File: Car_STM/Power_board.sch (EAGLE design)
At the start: 38 parts, among them K1 G2RE, K10 HY1-12V, K11 HY1-12V, K12 G2RE, K13 G2RE, K14 TF2-L2-9V, K2 HY1-12V, K3 TF2-L2-9V, K4 S22, K5 S22, K6 S22, K7 S22, K8 S22, K9 S22, X11 1751248, X13 1751248, X17 1751251, X18 1751251

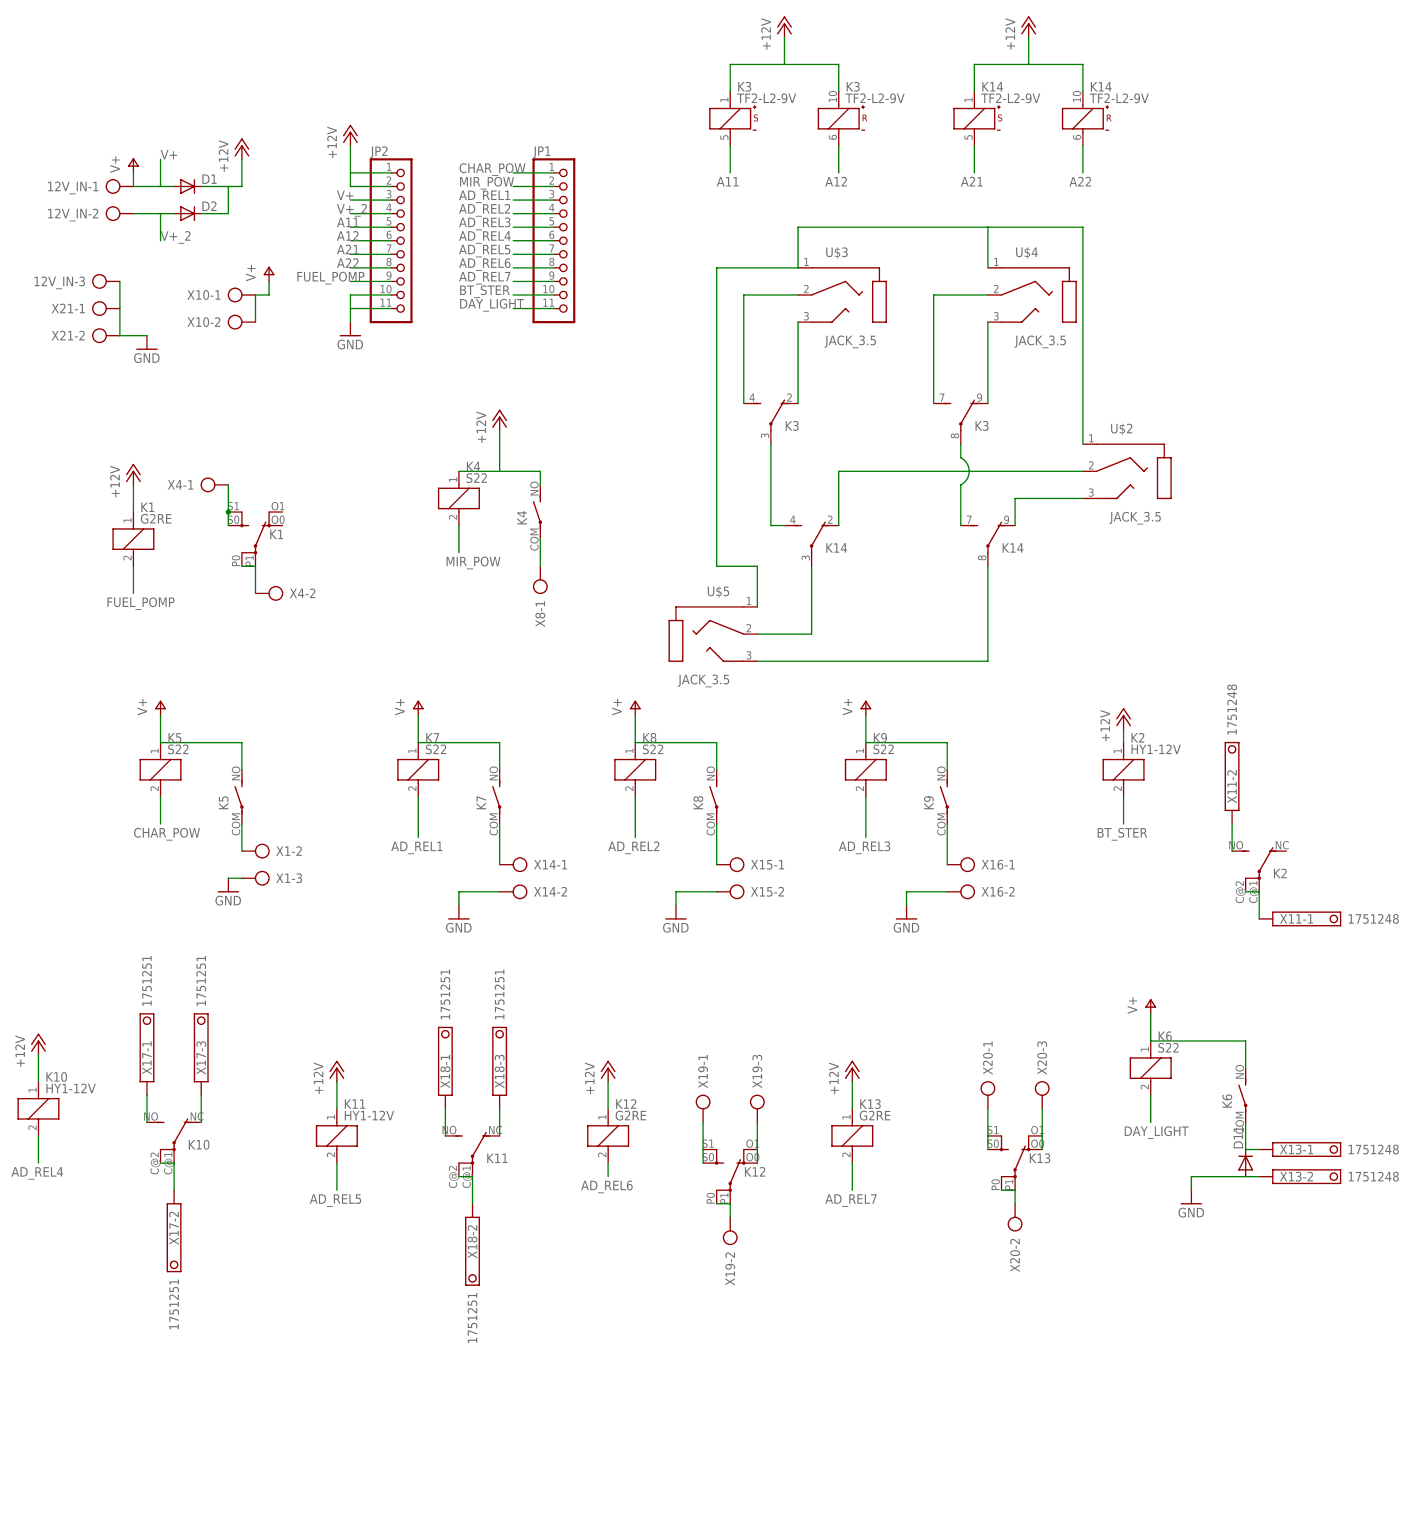
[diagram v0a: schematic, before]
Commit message: V1.21 New BT, audio, big cap on 12V
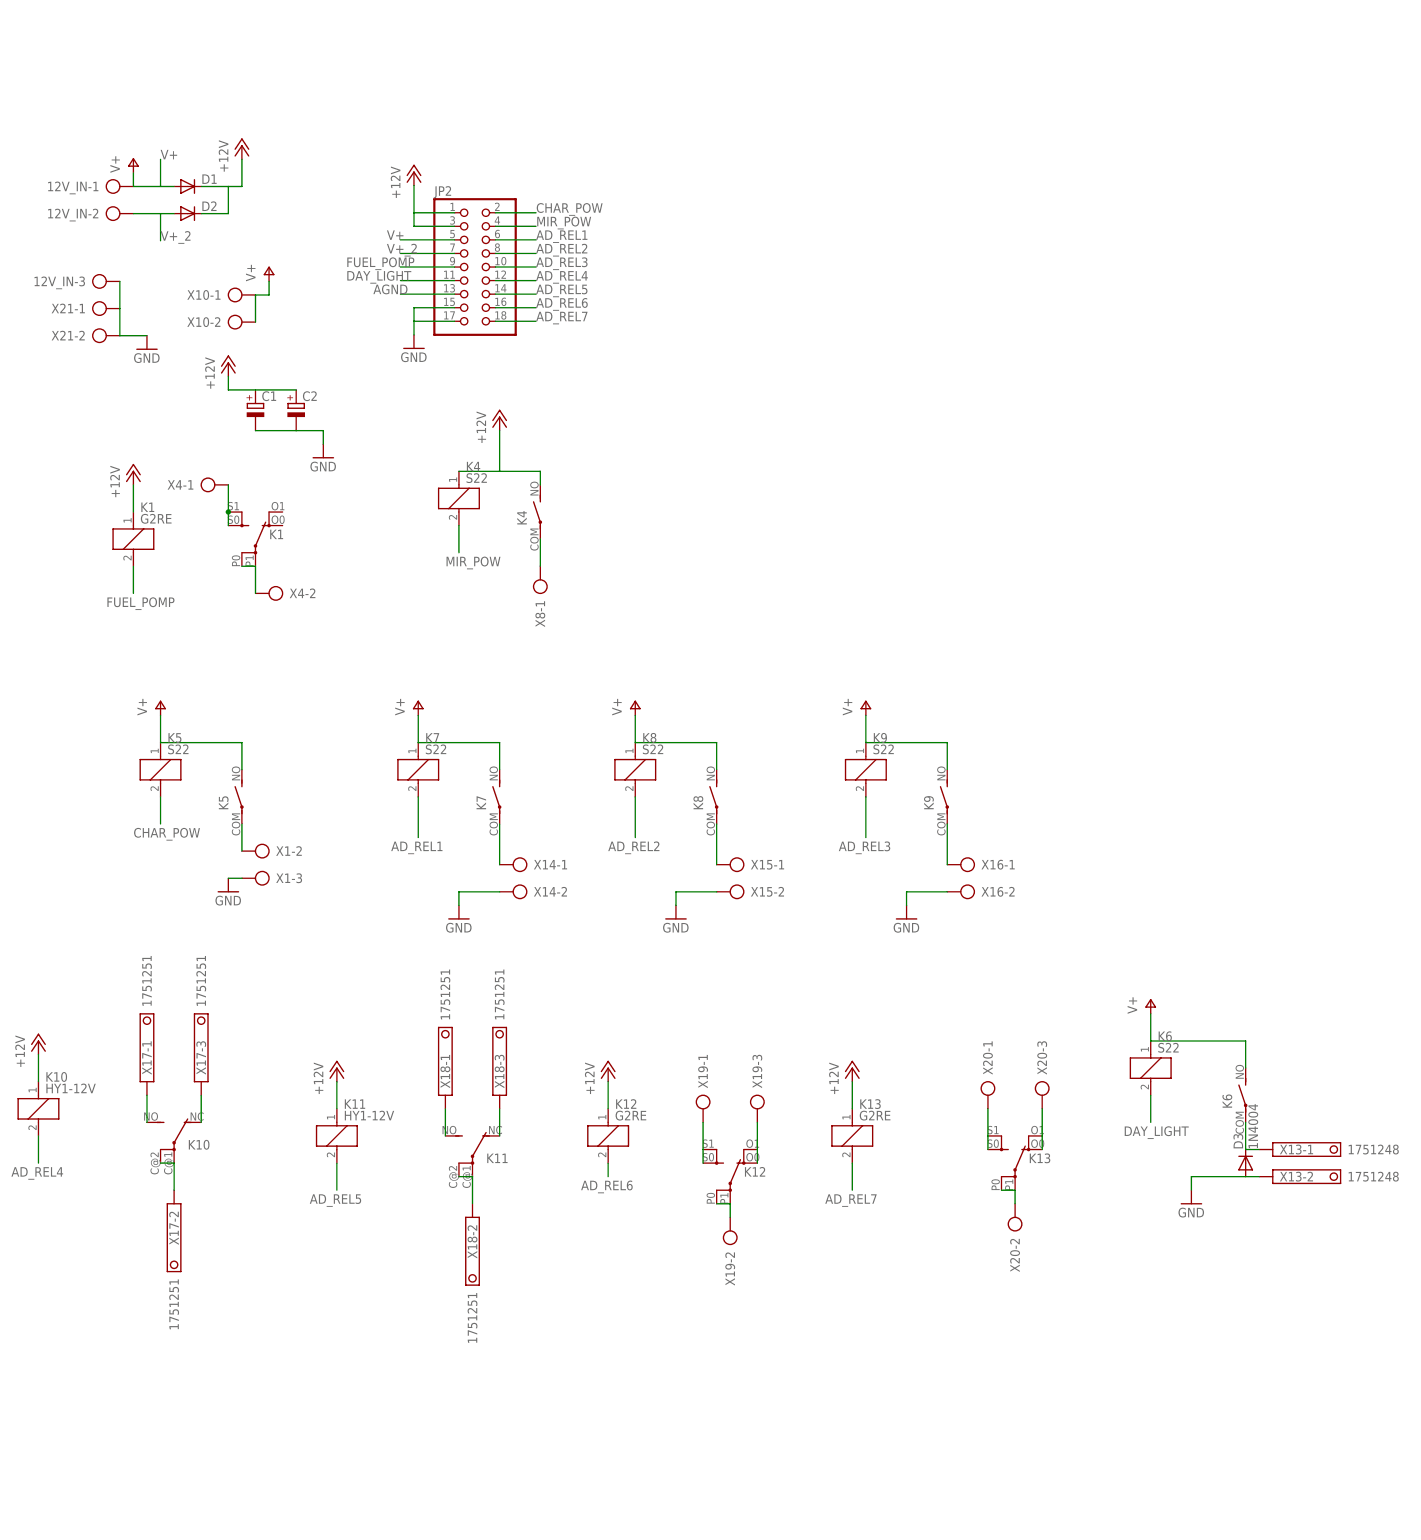
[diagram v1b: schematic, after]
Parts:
- removed D11: (no value), diode:DIODE-DO-214AC
- removed JP1: (no value), pinhead:PINHD-1X11
- removed K14, K3: TF2-L2-9V, relay:TF2-L2-9V
- removed K2: HY1-12V, relay:HY1-12V
- removed U$2, U$3, U$4, U$5: JACK_3.5, Stworzone:JACK_3.5
- removed X11: 1751248, con-phoenix-350:1751248
- added C1, C2: (no value), Stworzone:CAP_HORIZ
- added D3: 1N4004, diode:1N4004
- JP2: device pinhead:PINHD-1X11 -> pinhead:PINHD-2X9
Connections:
- removed net A11: JP2.5, K3S.-
- removed net A12: JP2.6, K3R.-
- removed net A21: JP2.7, K14S.-
- removed net A22: JP2.8, K14R.-
- removed net BT_STER: JP1.10, K21.2
- removed net N$100: K141.P, U$5.2
- removed net N$101: K142.P, U$5.5
- removed net N$57: K22.S, X11-2.K
- removed net N$58: K22.P, K22.P@1, X11-1.K
- removed net N$91: K141.O, U$2.2
- removed net N$92: K142.O, U$2.5
- removed net N$93: K142.S, K32.P
- removed net N$94: K141.S, K31.P
- removed net N$95: K31.S, U$3.2
- removed net N$96: K31.O, U$3.5
- removed net N$97: K32.S, U$4.2
- removed net N$98: K32.O, U$4.5
- removed net N$99: U$2.1, U$3.1, U$4.1, U$5.1
- new net AGND: JP2.13
- net +12V: now also C1.+, C2.+, JP2.3; no longer JP2.2, K14R.+, K14S.+, K21.1, K3R.+, K3S.+
- net AD_REL1: now also JP2.6; no longer JP1.3
- net AD_REL2: now also JP2.8; no longer JP1.4
- net AD_REL3: now also JP2.10; no longer JP1.5
- net AD_REL4: now also JP2.12; no longer JP1.6
- net AD_REL5: now also JP2.14; no longer JP1.7
- net AD_REL6: now also JP2.16; no longer JP1.8
- net AD_REL7: now also JP2.18; no longer JP1.9
- net CHAR_POW: now also JP2.2; no longer JP1.1
- net DAY_LIGHT: now also JP2.11; no longer JP1.11
- net GND: now also C1.-, C2.-, D3.A, JP2.15, JP2.17; no longer D11.A, JP2.10, JP2.11
- net MIR_POW: now also JP2.4; no longer JP1.2
- net N$54: now also D3.C; no longer D11.C
- net V+: now also JP2.5; no longer JP2.3
- net V+_2: now also JP2.7; no longer JP2.4

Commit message: V1.22 Logic board in progress
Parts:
- removed 12V_IN, X20: (no value), con-ptr500:AK500/3
- removed K12, K13: G2RE, relay:G2RE
- removed X16: (no value), con-ptr500:AK500/2
- added K2: G2RE, relay:G2RE
- added K3: S22, Stworzone:S22
- added X2: (no value), con-ptr500:AK500/2
- added X5: (no value), con-ptr500:AK500/3
- K1: value G2RE -> S22; device relay:G2RE -> Stworzone:S22
- K10, K11: value HY1-12V -> G2RE; device relay:HY1-12V -> relay:G2RE
- K8, K9: value S22 -> HY1-12V; device Stworzone:S22 -> relay:HY1-12V
- X10: device con-ptr500:AK500/2 -> con-ptr500:AK500/3
- X8: device con-ptr500:AK500/3 -> con-ptr500:AK500/2
- renumbered JP2 to JP1, X14 to X6, X15 to X7, X17 to X9, X18 to X11, X19 to X12, X21 to X3
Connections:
- net +12V: now also K1G$1.S, K1G$2.1, K21.1, K3G$2.1, K5G$2.1, K6G$2.1, K7G$2.1, K81.1, K91.1; no longer K11.1, K121.1, K131.1, K4G$1.S
- net AD_REL1: now also K4G$2.2; no longer K7G$2.2
- net AD_REL2: now also K5G$2.2; no longer K8G$2.2
- net AD_REL3: now also K6G$2.2; no longer K9G$2.2
- net AD_REL4: now also K81.2; no longer K101.2
- net AD_REL5: now also K91.2; no longer K111.2
- net AD_REL6: now also K101.2; no longer K121.2
- net AD_REL7: now also K111.2; no longer K131.2
- net CHAR_POW: now also K3G$2.2; no longer K5G$2.2
- net DAY_LIGHT: now also K7G$2.2; no longer K6G$2.2
- net FUEL_POMP: now also K21.2; no longer K11.2
- net GND: now also X5-3.KL, X8-2.KL; no longer 12V_IN-3.KL, X16-2.KL
- net MIR_POW: now also K1G$2.2; no longer K4G$2.2
- net N$18: now also K22.S, K22.S@1; no longer K12.S, K12.S@1
- net N$19: now also K22.P, K22.P@1; no longer K12.P, K12.P@1
- net N$48: now also K1G$1.P, X5-1.KL; no longer K4G$1.P, X8-1.KL
- net N$54: now also K7G$1.P; no longer K6G$1.P
- net N$64: now also K3G$1.P, X5-2.KL; no longer K5G$1.P, X1-2.KL
- net N$65: now also K4G$1.P; no longer K7G$1.P
- net N$69: now also K5G$1.P; no longer K8G$1.P
- net N$73: now also K6G$1.P, X8-1.KL; no longer K9G$1.P, X16-1.KL
- net N$76: now also K82.S; no longer K102.S
- net N$79: now also K82.O; no longer K102.O
- net N$81: now also K82.P, K82.P@1; no longer K102.P, K102.P@1
- net N$82: now also K92.S; no longer K112.S
- net N$83: now also K92.O; no longer K112.O
- net N$84: now also K92.P, K92.P@1; no longer K112.P, K112.P@1
- net N$85: now also K102.S, K102.S@1; no longer K122.S, K122.S@1
- net N$86: now also K102.O, K102.O@1; no longer K122.O, K122.O@1
- net N$87: now also K102.P, K102.P@1; no longer K122.P, K122.P@1
- net N$88: now also K112.S, K112.S@1, X10-1.KL; no longer K132.S, K132.S@1, X20-1.KL
- net N$89: now also K112.O, K112.O@1, X10-3.KL; no longer K132.O, K132.O@1, X20-3.KL
- net N$90: now also K112.P, K112.P@1, X10-2.KL; no longer K132.P, K132.P@1, X20-2.KL
- net V+: now also K3G$1.S, K4G$1.S, X1-1.KL, X2-1.KL, X2-2.KL; no longer 12V_IN-1.KL, K5G$2.1, K6G$2.1, K7G$2.1, K8G$1.S, K8G$2.1, K9G$1.S, K9G$2.1, X10-1.KL, X10-2.KL
- net V+_2: now also X1-2.KL; no longer 12V_IN-2.KL
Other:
- moved on the sheet: K10, K11, K4, K5, K6, K7, X1-2, X1-3, X10-1, X10-2, X8-1

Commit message: V1.24 First version of boards ended
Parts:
- added I1: ISOLATE, Stworzone:ISOLATE
- added JP2: (no value), jumper:JP2E
- added Q2: IRFR5305, transistor-power:IRFR5305
- added R3: 100k, resistor:R-EU_R0805
- added X14: (no value), con-phoenix-254:MPT3
- added X15: (no value), con-phoenix-254:MPT2
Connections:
- removed net N$48: K1G$1.P, X5-1.KL
- removed net N$64: K3G$1.P, X5-2.KL
- removed net N$65: K4G$1.P, X6-1.KL
- removed net N$69: K5G$1.P, X7-1.KL
- removed net N$73: K6G$1.P, X8-1.KL
- new net N$1: K1G$1.S, X5-3.KL
- new net N$2: K4G$1.S, X6-1.KL
- new net N$3: K3G$1.S, X5-2.KL
- new net N$4: K5G$1.S, X7-1.KL
- new net N$44: JP2.3, Q2.G, R3.1
- new net N$5: K6G$1.S, X8-1.KL
- new net N$7: JP2.1, K101.2
- net +12V: now also K1G$1.P, Q2.S, R3.2; no longer K1G$1.S
- net AD_REL6: now also JP2.2; no longer K101.2
- net AGND: now also I1.2, JP1.17; no longer JP1.13
- net CHAR_POW: now also JP1.15; no longer JP1.2
- net GND: now also I1.1, JP1.2, JP1.4, X5-1.KL; no longer JP1.15, JP1.17, X5-3.KL
- net MIR_POW: now also JP1.13; no longer JP1.4
- net V+: now also JP1.7, K3G$1.P, K4G$1.P, K5G$1.P, K6G$1.P; no longer JP1.5, K3G$1.S, K4G$1.S, K5G$1.S, K6G$1.S
- net V+_2: now also JP1.5; no longer JP1.7
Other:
- moved on the sheet: JP1, K1, K10, K3, K4, K5, K6, X1-1, X1-2, X5-1, X5-3

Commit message: V1.25 Just tittle missing
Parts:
- removed JP2: (no value), jumper:JP2E
- removed R3: 100k, resistor:R-EU_R0805
- added Q1: IRFR5305, transistor-power:IRFR5305
- added U$1, U$2, U$3, U$4: SCREW_3.2, Stworzone:SCREW_3.2
- JP1: device pinhead:PINHD-2X9 -> pinhead:PINHD-2X10
- X14: device con-phoenix-254:MPT3 -> con-phoenix-254:MPT2
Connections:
- removed net AD_REL7: JP1.18, K111.2
- removed net N$44: JP2.3, Q2.G, R3.1
- removed net N$7: JP2.1, K101.2
- new net FAN: JP1.20, Q1.G
- new net GAS_BUTTON: JP1.14, K91.2
- new net N$6: Q1.D, X14-1.1
- new net N$9: Q2.D, X15-1.1
- new net PELTIER: JP1.17, Q2.G
- net +12V: now also Q1.S; no longer R3.2
- net AD_REL1: now also JP1.18, K111.2; no longer JP1.6, K4G$2.2
- net AD_REL2: now also JP1.16, K101.2; no longer JP1.8, K5G$2.2
- net AD_REL3: now also JP1.12, K81.2; no longer JP1.10, K6G$2.2
- net AD_REL4: now also JP1.6, K4G$2.2; no longer JP1.12, K81.2
- net AD_REL5: now also JP1.10, K6G$2.2; no longer JP1.14, K91.2
- net AD_REL6: now also JP1.8, K5G$2.2; no longer JP1.16, JP2.2
- net AGND: now also JP1.19; no longer JP1.17
- net GND: now also U$1.MOUNT, U$2.MOUNT, U$3.MOUNT, U$4.MOUNT, X14-2.1, X15-2.1
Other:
- moved on the sheet: D3, I1, K1, K10, K11, K3, K4, K5, K6, K7, K8, K9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
